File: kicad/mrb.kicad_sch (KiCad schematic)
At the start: 7 parts

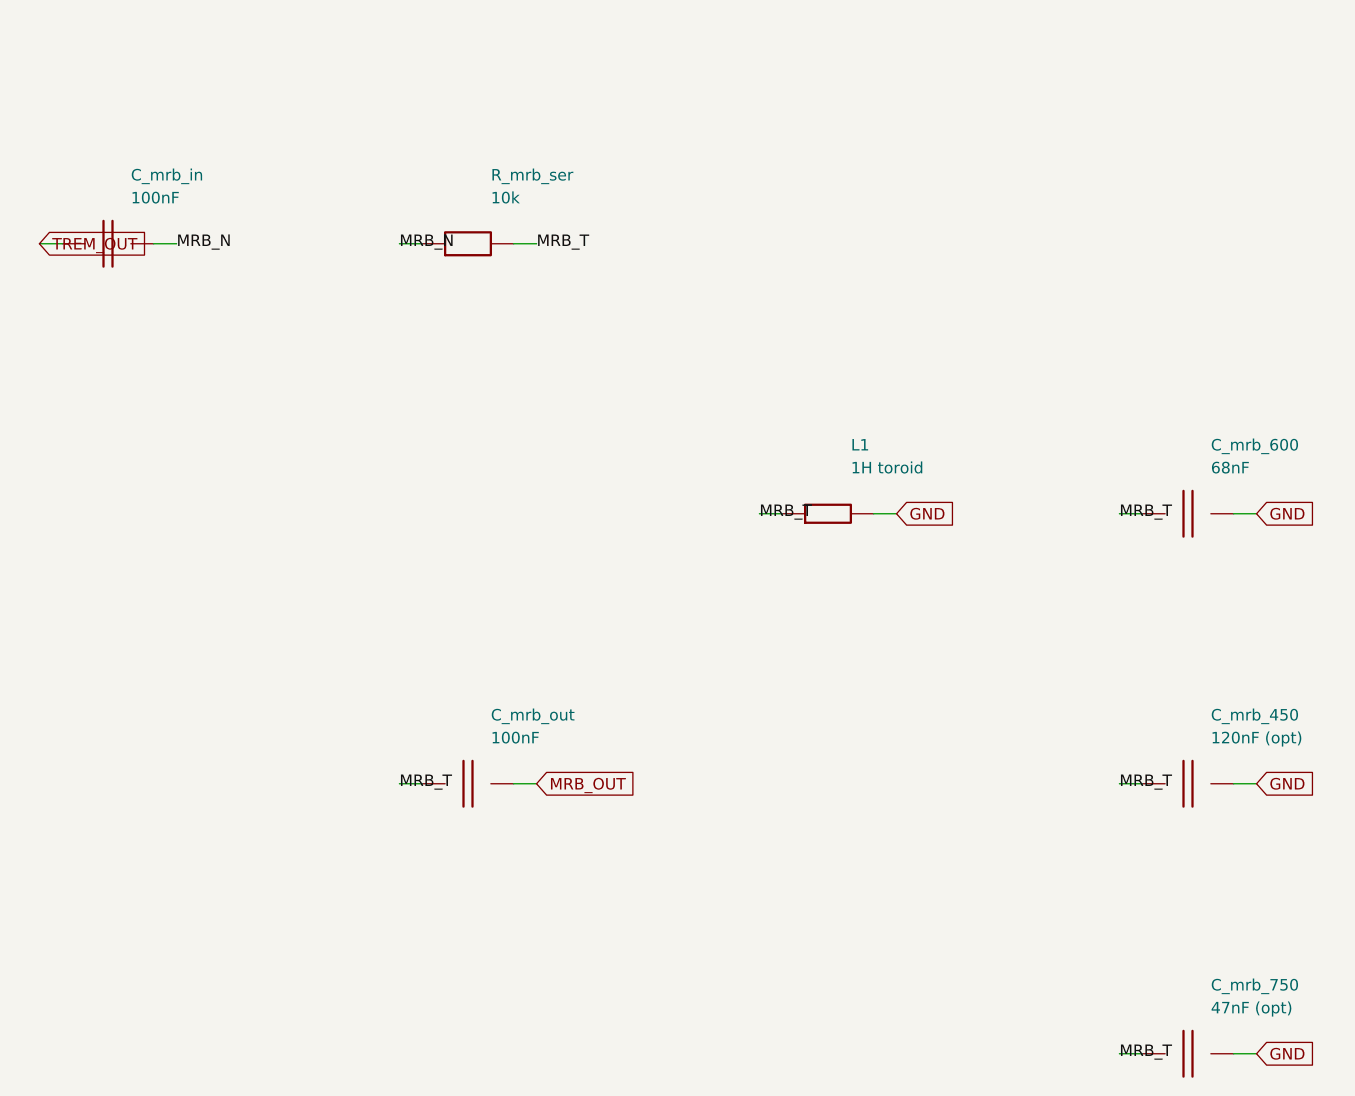
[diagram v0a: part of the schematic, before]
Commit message: Schematic passes KiCad 8 ERC (0 violations); add op-amp mid-rail bias
Installed KiCad 8.0.9 and ran a real Electrical Rules Check on the generated
hierarchy. Drove it to 0 violations:
- snapped every pin/wire endpoint to the 1.27 mm connection grid (was 338
  endpoint_off_grid violations)
- gave the footswitch lines FS_REV/FS_TREM/FS_MRB a real second endpoint via
  100k control pulldowns on the reverb/tremolo/mrb sheets (was 3 dangling labels)

Also made the single-supply TL072 stages electrically real: added a mid-rail
VBIAS network (R_vb1/R_vb2 + C_vb on the Power Supply sheet) and referenced the
reverb driver and tremolo LFO inputs/gain-returns to VBIAS instead of GND
(design addition, flagged in the sheet notes).

Result: kicad-cli 8.0.9 sch erc -> 0 violations; netlist 102 components, 58
nets, 0 unconnected pins; VBIAS spans 10 nodes. Updated SCHEMATIC-BUILD.md,
kicad/README.md, CHANGELOG.md.

https://claude.ai/code/session_01PkrfUi9tvZfLvudJ7h23qD
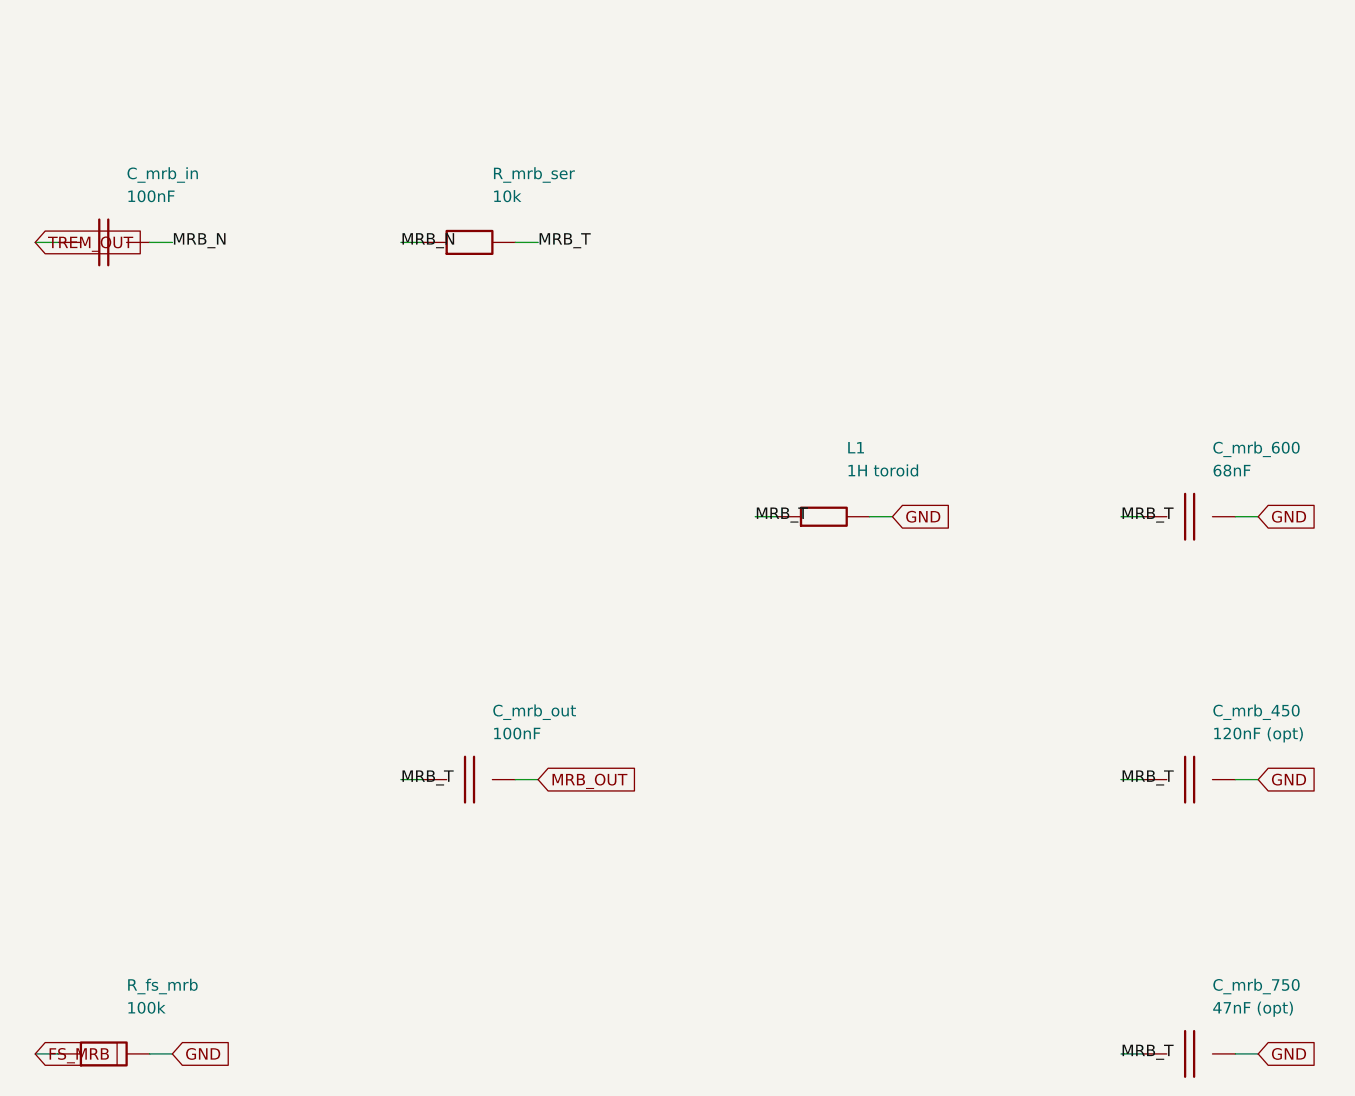
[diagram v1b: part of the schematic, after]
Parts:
- added R_fs_mrb: 100k, symbol cr_primitives:R
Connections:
- net GND: now also R_fs_mrb.2
- new net FS_MRB: R_fs_mrb.1

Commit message: Generate auto-placed PCB (102 footprints, GND pour, board outline)
Build cambridge_reverb.kicad_pcb from the schematic via kicad/gen/gen_pcb.py
(KiCad 8 pcbnew API): assign a THT footprint to every component (standard libs
for generics + the project footprints for VTL5C1 and the 1H toroid), place all
102 footprints (off-board connectors on a bottom wiring-edge strip, toroid in a
reserved spot), assign all 58 nets to pads, draw a 190x115 mm Edge.Cuts outline,
and pour a bottom-layer GND plane. Footprint assignments also carry into the
schematic symbols.

The board opens in KiCad and the ratsnest matches the ERC-clean schematic. It is
placed but NOT routed: kicad-cli pcb drc is dominated by 130 unconnected
(unrouted signal nets; GND is poured) plus cosmetic silk/courtyard overlaps from
dense auto-placement at chassis size -- documented in kicad/PCB-NOTES.md with the
remaining hand-work (placement into floor-plan zones, routing, DRC-to-zero,
Gerbers). Net classes (Default/Power/HighCurrent) carry over for routing.

Also: schematic resistor footprint switched to the compact vertical variant;
gitignore DRC/ERC .rpt reports.

https://claude.ai/code/session_01PkrfUi9tvZfLvudJ7h23qD
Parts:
- C_mrb_450, C_mrb_600, C_mrb_750, C_mrb_in, C_mrb_out: footprint (none) -> Capacitor_THT:C_Disc_D7.5mm_W2.5mm_P5.00mm
- L1: footprint (none) -> cambridge_reverb:Inductor_MRB_1H_Toroid
- R_fs_mrb, R_mrb_ser: footprint (none) -> Resistor_THT:R_Axial_DIN0207_L6.3mm_D2.5mm_P5.08mm_Vertical
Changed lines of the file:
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@@
     (property "Reference" "C_mrb_in" (at 52.07 62.23 0) (effects (font (size 1.27 1.27)) (justify left)))
     (property "Value" "100nF" (at 52.07 64.77 0) (effects (font (size 1.27 1.27)) (justify left)))
-    (property "Footprint" "" (at 49.53 69.85 0) (effects (font (size 1.27 1.27)) hide))
+    (property "Footprint" "Capacitor_THT:C_Disc_D7.5mm_W2.5mm_P5.00mm" (at 49.53 69.85 0) (effects (font (size 1.27 1.27)) hide))
     (pin "1")
     (pin "2")
-    (instances (project "cambridge_reverb" (path "/f05f6d70-f7ad-4410-afb7-cbbafabffaf9" (reference "C_mrb_in") (unit 1))))
+    (instances (project "cambridge_reverb" (path "/ffde72b1-ecdf-48d1-98aa-547fb4c9909d" (reference "C_mrb_in") (unit 1))))
   )
   (wire (pts (xy 44.45 69.85) (xy 41.910000000000004 69.85)) (stroke (width 0) (type default)))
@@
     (property "Reference" "R_mrb_ser" (at 92.71000000000001 62.23 0) (effects (font (size 1.27 1.27)) (justify left)))
     (property "Value" "10k" (at 92.71000000000001 64.77 0) (effects (font (size 1.27 1.27)) (justify left)))
-    (property "Footprint" "" (at 90.17 69.85 0) (effects (font (size 1.27 1.27)) hide))
+    (property "Footprint" "Resistor_THT:R_Axial_DIN0207_L6.3mm_D2.5mm_P5.08mm_Vertical" (at 90.17 69.85 0) (effects (font (size 1.27 1.27)) hide))
     (pin "1")
     (pin "2")
-    (instances (project "cambridge_reverb" (path "/f05f6d70-f7ad-4410-afb7-cbbafabffaf9" (reference "R_mrb_ser") (unit 1))))
+    (instances (project "cambridge_reverb" (path "/ffde72b1-ecdf-48d1-98aa-547fb4c9909d" (reference "R_mrb_ser") (unit 1))))
   )
   (wire (pts (xy 85.09 69.85) (xy 82.55 69.85)) (stroke (width 0) (type default)))
@@
     (property "Reference" "L1" (at 132.07999999999998 92.71 0) (effects (font (size 1.27 1.27)) (justify left)))
     (property "Value" "1H toroid" (at 132.07999999999998 95.25 0) (effects (font (size 1.27 1.27)) (justify left)))
-    (property "Footprint" "" (at 129.54 100.33 0) (effects (font (size 1.27 1.27)) hide))
+    (property "Footprint" "cambridge_reverb:Inductor_MRB_1H_Toroid" (at 129.54 100.33 0) (effects (font (size 1.27 1.27)) hide))
     (pin "1")
     (pin "2")
-    (instances (project "cambridge_reverb" (path "/f05f6d70-f7ad-4410-afb7-cbbafabffaf9" (reference "L1") (unit 1))))
+    (instances (project "cambridge_reverb" (path "/ffde72b1-ecdf-48d1-98aa-547fb4c9909d" (reference "L1") (unit 1))))
   )
   (wire (pts (xy 124.46 100.33) (xy 121.91999999999999 100.33)) (stroke (width 0) (type default)))
@@
     (property "Reference" "C_mrb_600" (at 172.72 92.71 0) (effects (font (size 1.27 1.27)) (justify left)))
     (property "Value" "68nF" (at 172.72 95.25 0) (effects (font (size 1.27 1.27)) (justify left)))
-    (property "Footprint" "" (at 170.18 100.33 0) (effects (font (size 1.27 1.27)) hide))
+    (property "Footprint" "Capacitor_THT:C_Disc_D7.5mm_W2.5mm_P5.00mm" (at 170.18 100.33 0) (effects (font (size 1.27 1.27)) hide))
     (pin "1")
     (pin "2")
-    (instances (project "cambridge_reverb" (path "/f05f6d70-f7ad-4410-afb7-cbbafabffaf9" (reference "C_mrb_600") (unit 1))))
+    (instances (project "cambridge_reverb" (path "/ffde72b1-ecdf-48d1-98aa-547fb4c9909d" (reference "C_mrb_600") (unit 1))))
   )
   (wire (pts (xy 165.1 100.33) (xy 162.56 100.33)) (stroke (width 0) (type default)))
@@
     (property "Reference" "C_mrb_450" (at 172.72 121.91999999999999 0) (effects (font (size 1.27 1.27)) (justify left)))
     (property "Value" "120nF (opt)" (at 172.72 124.46 0) (effects (font (size 1.27 1.27)) (justify left)))
-    (property "Footprint" "" (at 170.18 129.54 0) (effects (font (size 1.27 1.27)) hide))
+    (property "Footprint" "Capacitor_THT:C_Disc_D7.5mm_W2.5mm_P5.00mm" (at 170.18 129.54 0) (effects (font (size 1.27 1.27)) hide))
     (pin "1")
     (pin "2")
-    (instances (project "cambridge_reverb" (path "/f05f6d70-f7ad-4410-afb7-cbbafabffaf9" (reference "C_mrb_450") (unit 1))))
+    (instances (project "cambridge_reverb" (path "/ffde72b1-ecdf-48d1-98aa-547fb4c9909d" (reference "C_mrb_450") (unit 1))))
   )
   (wire (pts (xy 165.1 129.54) (xy 162.56 129.54)) (stroke (width 0) (type default)))
@@
     (property "Reference" "C_mrb_750" (at 172.72 152.4 0) (effects (font (size 1.27 1.27)) (justify left)))
     (property "Value" "47nF (opt)" (at 172.72 154.94 0) (effects (font (size 1.27 1.27)) (justify left)))
-    (property "Footprint" "" (at 170.18 160.02 0) (effects (font (size 1.27 1.27)) hide))
+    (property "Footprint" "Capacitor_THT:C_Disc_D7.5mm_W2.5mm_P5.00mm" (at 170.18 160.02 0) (effects (font (size 1.27 1.27)) hide))
     (pin "1")
     (pin "2")
-    (instances (project "cambridge_reverb" (path "/f05f6d70-f7ad-4410-afb7-cbbafabffaf9" (reference "C_mrb_750") (unit 1))))
+    (instances (project "cambridge_reverb" (path "/ffde72b1-ecdf-48d1-98aa-547fb4c9909d" (reference "C_mrb_750") (unit 1))))
   )
   (wire (pts (xy 165.1 160.02) (xy 162.56 160.02)) (stroke (width 0) (type default)))
@@
     (property "Reference" "C_mrb_out" (at 92.71000000000001 121.91999999999999 0) (effects (font (size 1.27 1.27)) (justify left)))
     (property "Value" "100nF" (at 92.71000000000001 124.46 0) (effects (font (size 1.27 1.27)) (justify left)))
-    (property "Footprint" "" (at 90.17 129.54 0) (effects (font (size 1.27 1.27)) hide))
+    (property "Footprint" "Capacitor_THT:C_Disc_D7.5mm_W2.5mm_P5.00mm" (at 90.17 129.54 0) (effects (font (size 1.27 1.27)) hide))
     (pin "1")
     (pin "2")
-    (instances (project "cambridge_reverb" (path "/f05f6d70-f7ad-4410-afb7-cbbafabffaf9" (reference "C_mrb_out") (unit 1))))
+    (instances (project "cambridge_reverb" (path "/ffde72b1-ecdf-48d1-98aa-547fb4c9909d" (reference "C_mrb_out") (unit 1))))
   )
   (wire (pts (xy 85.09 129.54) (xy 82.55 129.54)) (stroke (width 0) (type default)))
@@
     (property "Reference" "R_fs_mrb" (at 52.07 152.4 0) (effects (font (size 1.27 1.27)) (justify left)))
     (property "Value" "100k" (at 52.07 154.94 0) (effects (font (size 1.27 1.27)) (justify left)))
-    (property "Footprint" "" (at 49.53 160.02 0) (effects (font (size 1.27 1.27)) hide))
+    (property "Footprint" "Resistor_THT:R_Axial_DIN0207_L6.3mm_D2.5mm_P5.08mm_Vertical" (at 49.53 160.02 0) (effects (font (size 1.27 1.27)) hide))
     (pin "1")
     (pin "2")
-    (instances (project "cambridge_reverb" (path "/f05f6d70-f7ad-4410-afb7-cbbafabffaf9" (reference "R_fs_mrb") (unit 1))))
+    (instances (project "cambridge_reverb" (path "/ffde72b1-ecdf-48d1-98aa-547fb4c9909d" (reference "R_fs_mrb") (unit 1))))
   )
   (wire (pts (xy 44.45 160.02) (xy 41.910000000000004 160.02)) (stroke (width 0) (type default)))
